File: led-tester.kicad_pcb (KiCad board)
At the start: 2 copper layers, 38.8 x 44.2 mm, 35 parts, among them M1 Arduino_Mini, Q1 MMBT3904, U1 PCF8591, U2 LMV358

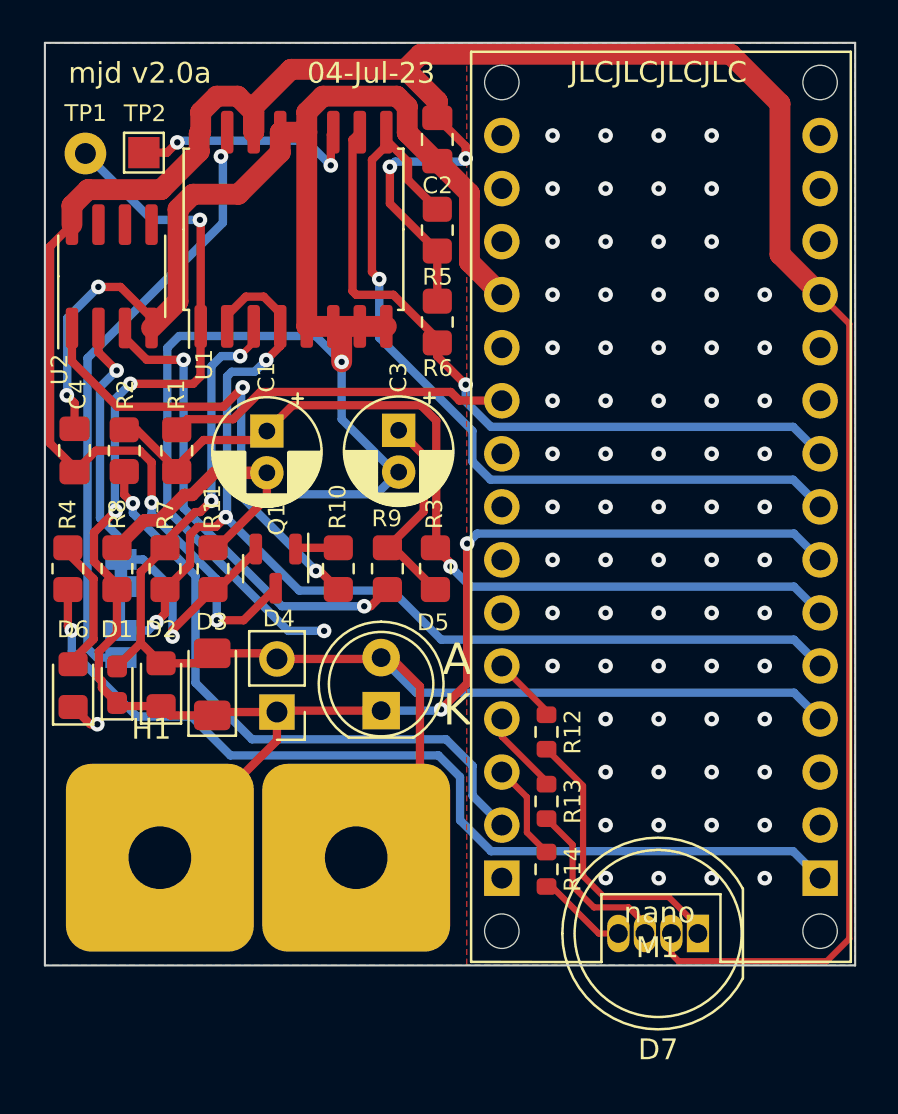
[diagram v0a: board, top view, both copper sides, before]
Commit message: Hide RGB LED and resistors from 3d view, and move designators
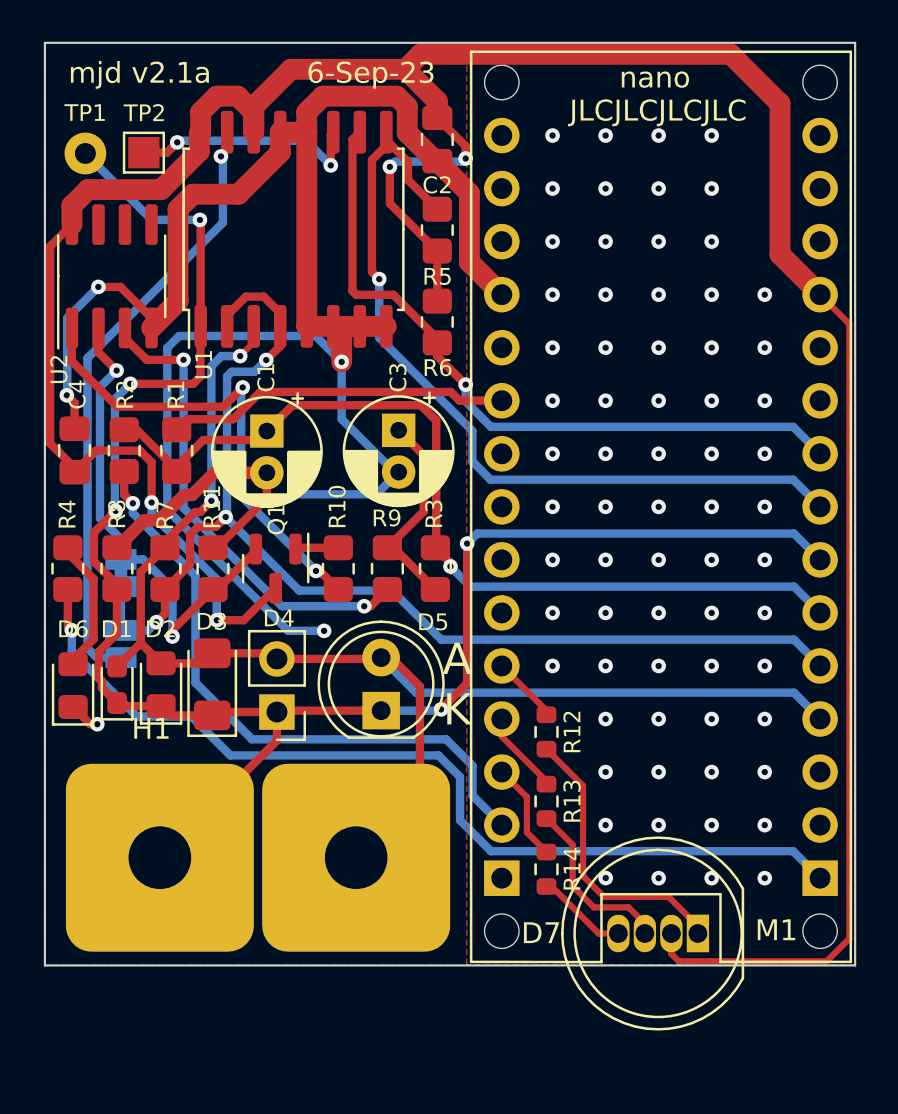
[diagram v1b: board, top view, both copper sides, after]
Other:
- board text added: "6-Sep-23"
- board text added: "mjd v2.1a"
- board text removed: "04-Jul-23"
- board text removed: "mjd v2.0a"
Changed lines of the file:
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@@
     )
     (pad_to_mask_clearance 0)
-    (aux_axis_origin 100 100)
-    (grid_origin 163.25 127)
+    (aux_axis_origin 0 0)
+    (grid_origin 133.48 84.11)
     (pcbplotparams
       (layerselection 0x00010fc_ffffffff)
@@
     (property "ki_keywords" "connector")
     (attr through_hole)
-    (fp_text reference "M1" (at 1.2 -21.1) (layer "F.SilkS")
+    (fp_text reference "M1" (at -4.5 -20.29) (layer "F.SilkS")
         (effects (font (size 1 1) (thickness 0.15)) (justify left))
     )
@@
       (net 22 "/D13{slash}SCK") (pinfunction "D13") (pintype "passive"))
     (pad "GND" thru_hole oval (at -7.62 15.24 180) (size 1.7 1.7) (drill 1) (layers "*.Cu" "*.Mask")
-      (net 1 "GND") (pinfunction "GND") (pintype "passive"))
+      (net 1 "GND") (pinfunction "GND") (pintype "power_out"))
     (pad "GND" thru_hole oval (at 7.62 10.16 180) (size 1.7 1.7) (drill 1) (layers "*.Cu" "*.Mask")
-      (net 1 "GND") (pinfunction "GND") (pintype "passive"))
+      (net 1 "GND") (pinfunction "GND") (pintype "power_out"))
     (pad "RESET" thru_hole oval (at -7.62 12.7 180) (size 1.7 1.7) (drill 1) (layers "*.Cu" "*.Mask")
-      (net 2 "/~{RESET}") (pinfunction "RESET") (pintype "passive"))
+      (net 2 "/~{RESET}") (pinfunction "RESET") (pintype "passive+no_connect"))
     (pad "RESET" thru_hole oval (at 7.62 12.7 180) (size 1.7 1.7) (drill 1) (layers "*.Cu" "*.Mask")
-      (net 2 "/~{RESET}") (pinfunction "RESET") (pintype "passive"))
+      (net 2 "/~{RESET}") (pinfunction "RESET") (pintype "passive+no_connect"))
     (pad "VIN" thru_hole oval (at -7.62 17.78 180) (size 1.7 1.7) (drill 1) (layers "*.Cu" "*.Mask")
       (net 30 "unconnected-(M1-PadVIN)") (pinfunction "VIN") (pintype "passive+no_connect"))
@@
     (property "ki_description" "Resistor")
     (property "ki_keywords" "R res resistor")
-    (attr smd)
+    (attr smd exclude_from_pos_files)
     (fp_text reference "R14" (at 0 1.25 90) (layer "F.SilkS")
         (effects (font (size 0.8 0.8) (thickness 0.12)))
@@
     (property "ki_description" "RGB LED, red/anode/green/blue")
     (property "ki_keywords" "LED RGB diode")
-    (attr through_hole)
-    (fp_text reference "D7" (at 1.905 -5.56) (layer "F.SilkS")
+    (attr through_hole exclude_from_pos_files)
+    (fp_text reference "D7" (at 7.5 0) (layer "F.SilkS")
         (effects (font (size 1 1) (thickness 0.15)))
     )
@@
     (property "ki_description" "Resistor")
     (property "ki_keywords" "R res resistor")
-    (attr smd)
+    (attr smd exclude_from_pos_files)
     (fp_text reference "R12" (at 0 1.25 90) (layer "F.SilkS")
         (effects (font (size 0.8 0.8) (thickness 0.12)))
@@
     (property "ki_description" "Resistor")
     (property "ki_keywords" "R res resistor")
-    (attr smd)
+    (attr smd exclude_from_pos_files)
     (fp_text reference "R13" (at 0 1.25 90) (layer "F.SilkS")
         (effects (font (size 0.8 0.8) (thickness 0.12)))
@@
   (gr_rect (start 133.48 84.1) (end 172.28 128.28)
     (stroke (width 0.1) (type default)) (fill none) (layer "Edge.Cuts"))
-  (gr_text "nano" (at 161.2 126.34) (layer "F.SilkS")
+  (gr_text "nano" (at 160.98 86.36) (layer "F.SilkS")
     (effects (font (size 1 1) (thickness 0.15)) (justify left bottom))
   )
-  (gr_text "mjd v2.0a" (at 138.03 85.55) (layer "F.SilkS")
+  (gr_text "mjd v2.1a" (at 138.03 85.55) (layer "F.SilkS")
     (effects (font (size 1 1) (thickness 0.15)))
   )
-  (gr_text "JLCJLCJLCJLC" (at 162.85 85.51) (layer "F.SilkS")
+  (gr_text "JLCJLCJLCJLC" (at 162.85 87.36) (layer "F.SilkS")
     (effects (font (size 1 1) (thickness 0.15)))
   )
@@
     (effects (font (size 1.5 1.5) (thickness 0.2)))
   )
-  (gr_text "04-Jul-23" (at 149.1 85.55) (layer "F.SilkS")
+  (gr_text "6-Sep-23" (at 149.1 85.55) (layer "F.SilkS")
     (effects (font (size 1 1) (thickness 0.15)))
   )

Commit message: News caps plus tweaks
Added SMD caps as alternatives to THT
Updated footprints from library
Separator on silk between power LED and test LEDs.
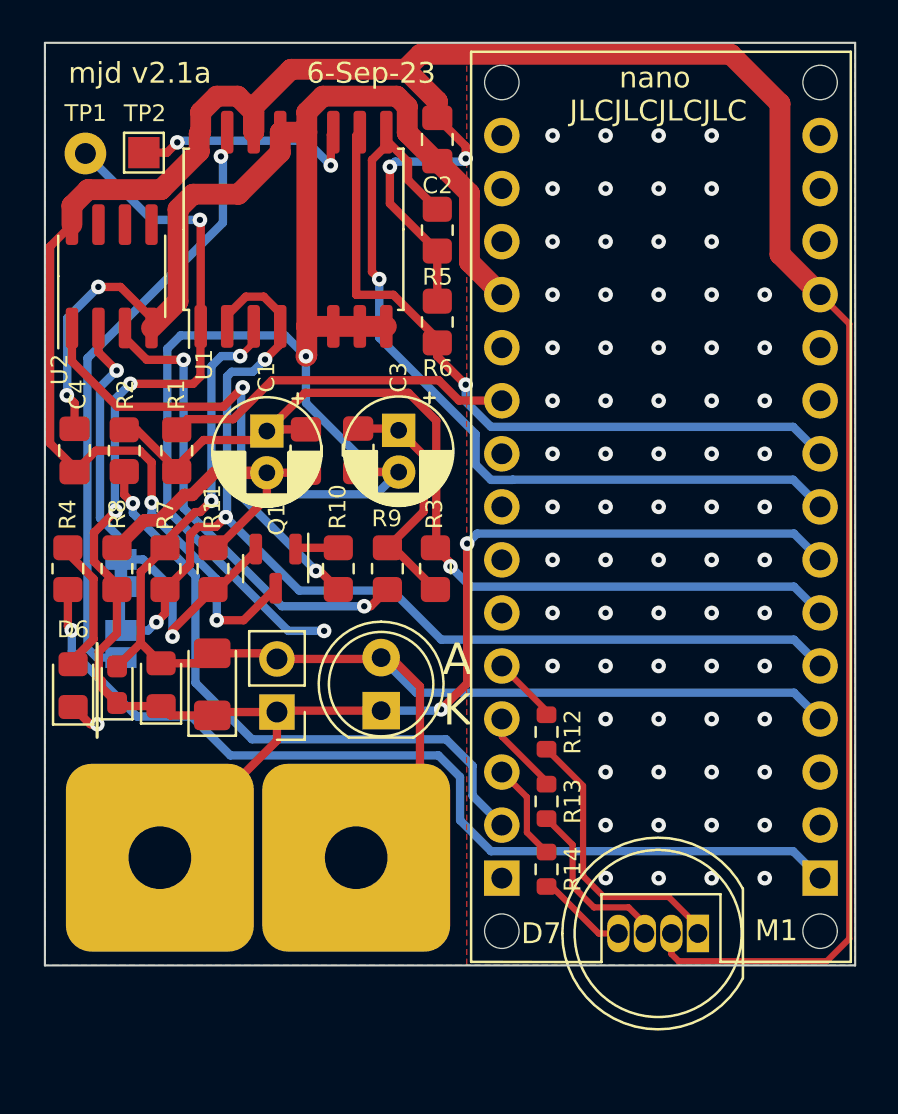
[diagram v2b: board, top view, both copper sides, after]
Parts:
- added C5: 10u, Capacitor_SMD:C_0805_2012Metric_Pad1.18x1.45mm_HandSolder, F.Cu at (146.0, 103.6)
- added C6: 10u, Capacitor_SMD:C_0805_2012Metric_Pad1.18x1.45mm_HandSolder, F.Cu at (148.5, 103.6)
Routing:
- net GND: track 111.5 -> 114.6 mm
- net /A2: track 43.5 -> 45.9 mm
- net Net-(C3-Pad1): track 9.97 -> 11.9 mm

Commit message: Oops, files that went to JLC did not have designators in silkscreen.
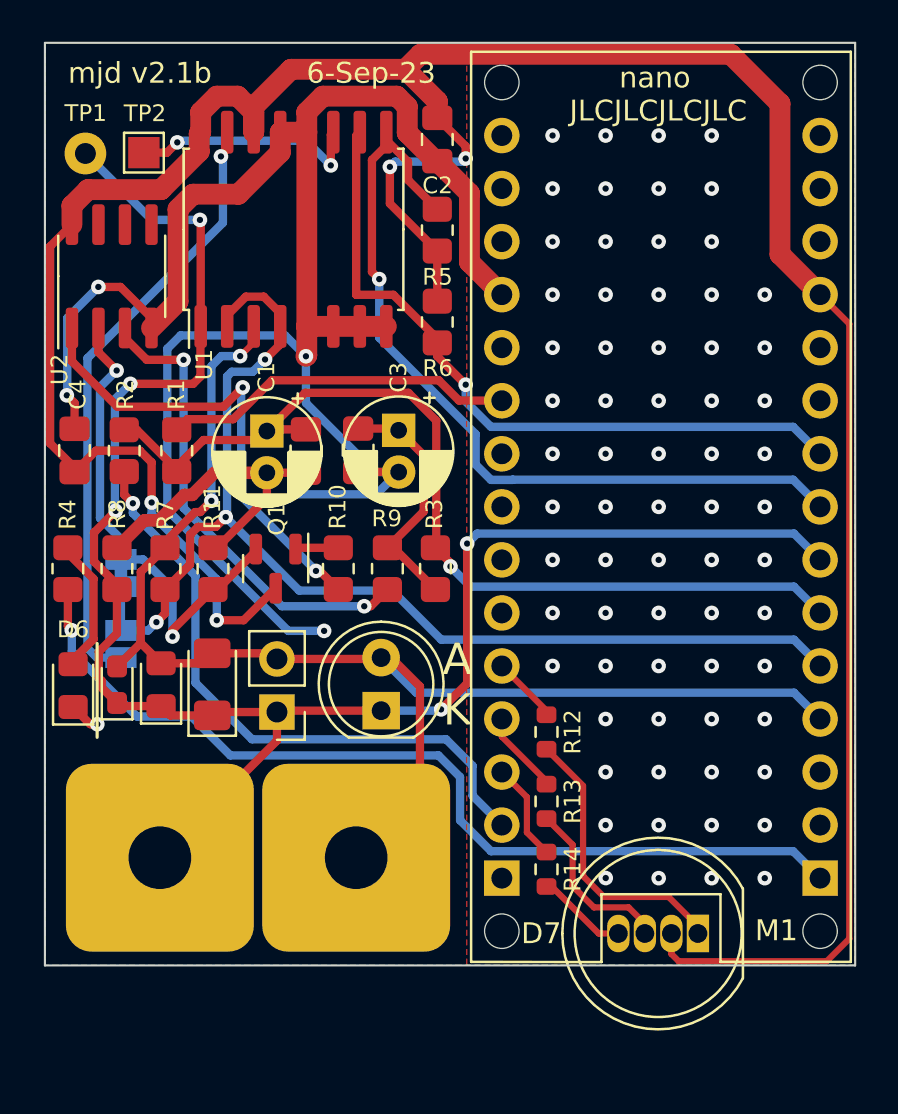
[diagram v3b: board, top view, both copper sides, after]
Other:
- board text added: "mjd v2.1b"
- board text removed: "mjd v2.1a"
